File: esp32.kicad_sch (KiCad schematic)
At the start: 8 parts, among them U1 ESP32-S3-WROOM-2, U4 74HC595, U6 TCA9548APWR

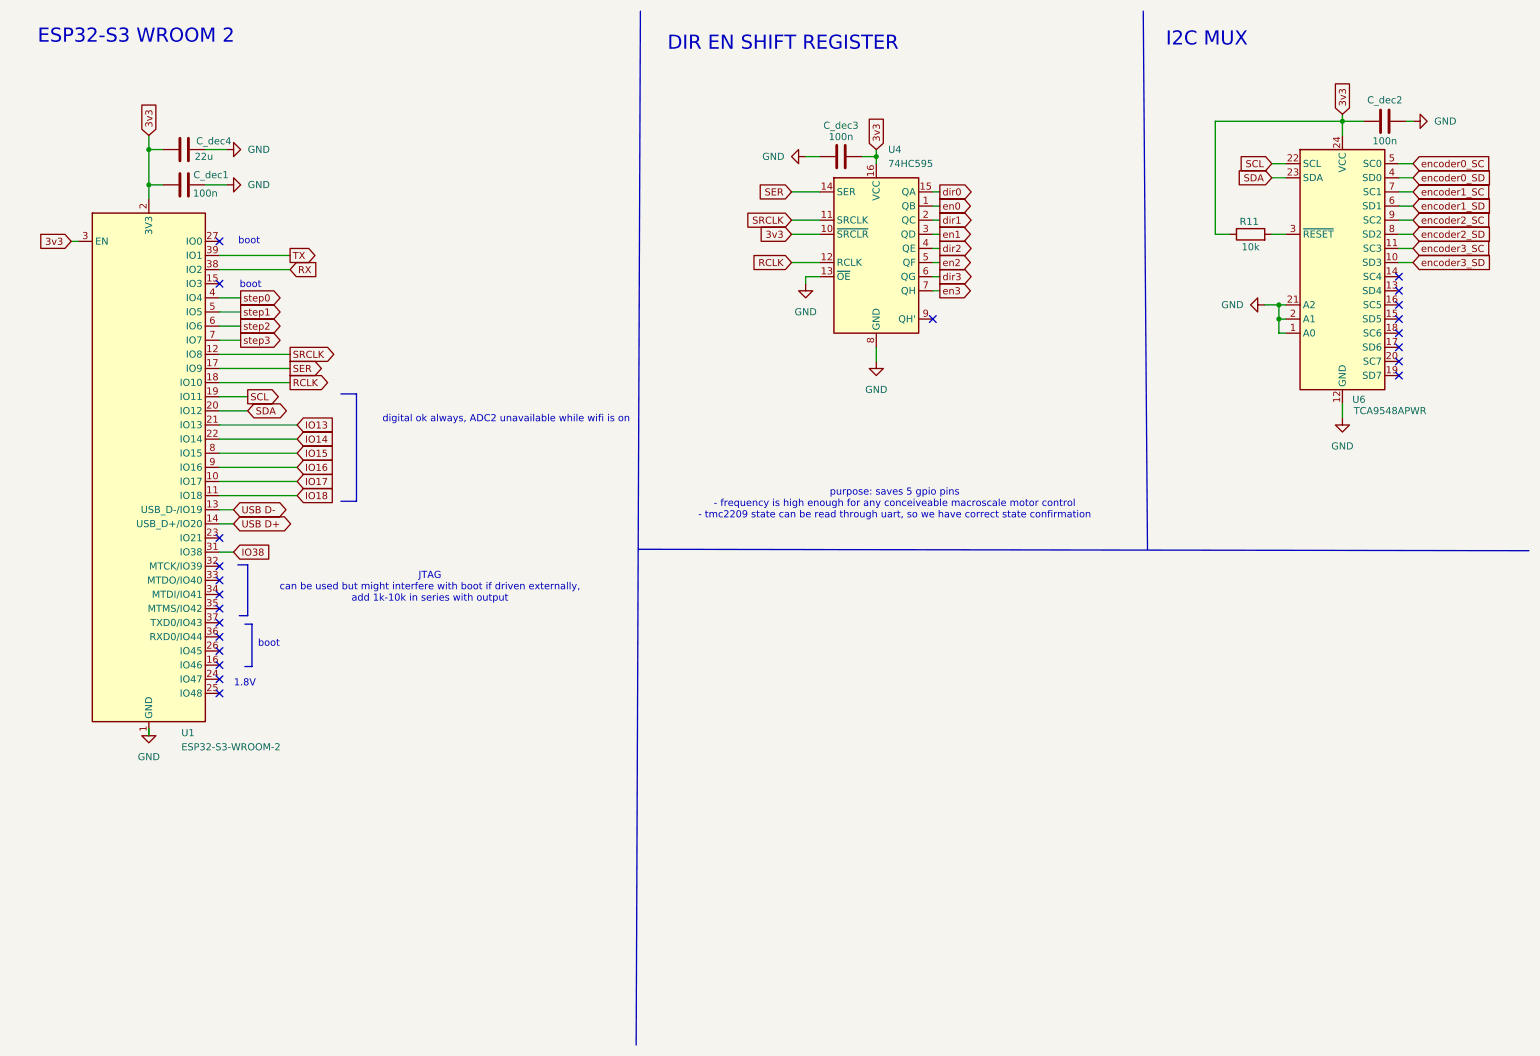
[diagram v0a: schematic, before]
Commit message: revision 1: I2C pullups, USB LDO, etc.
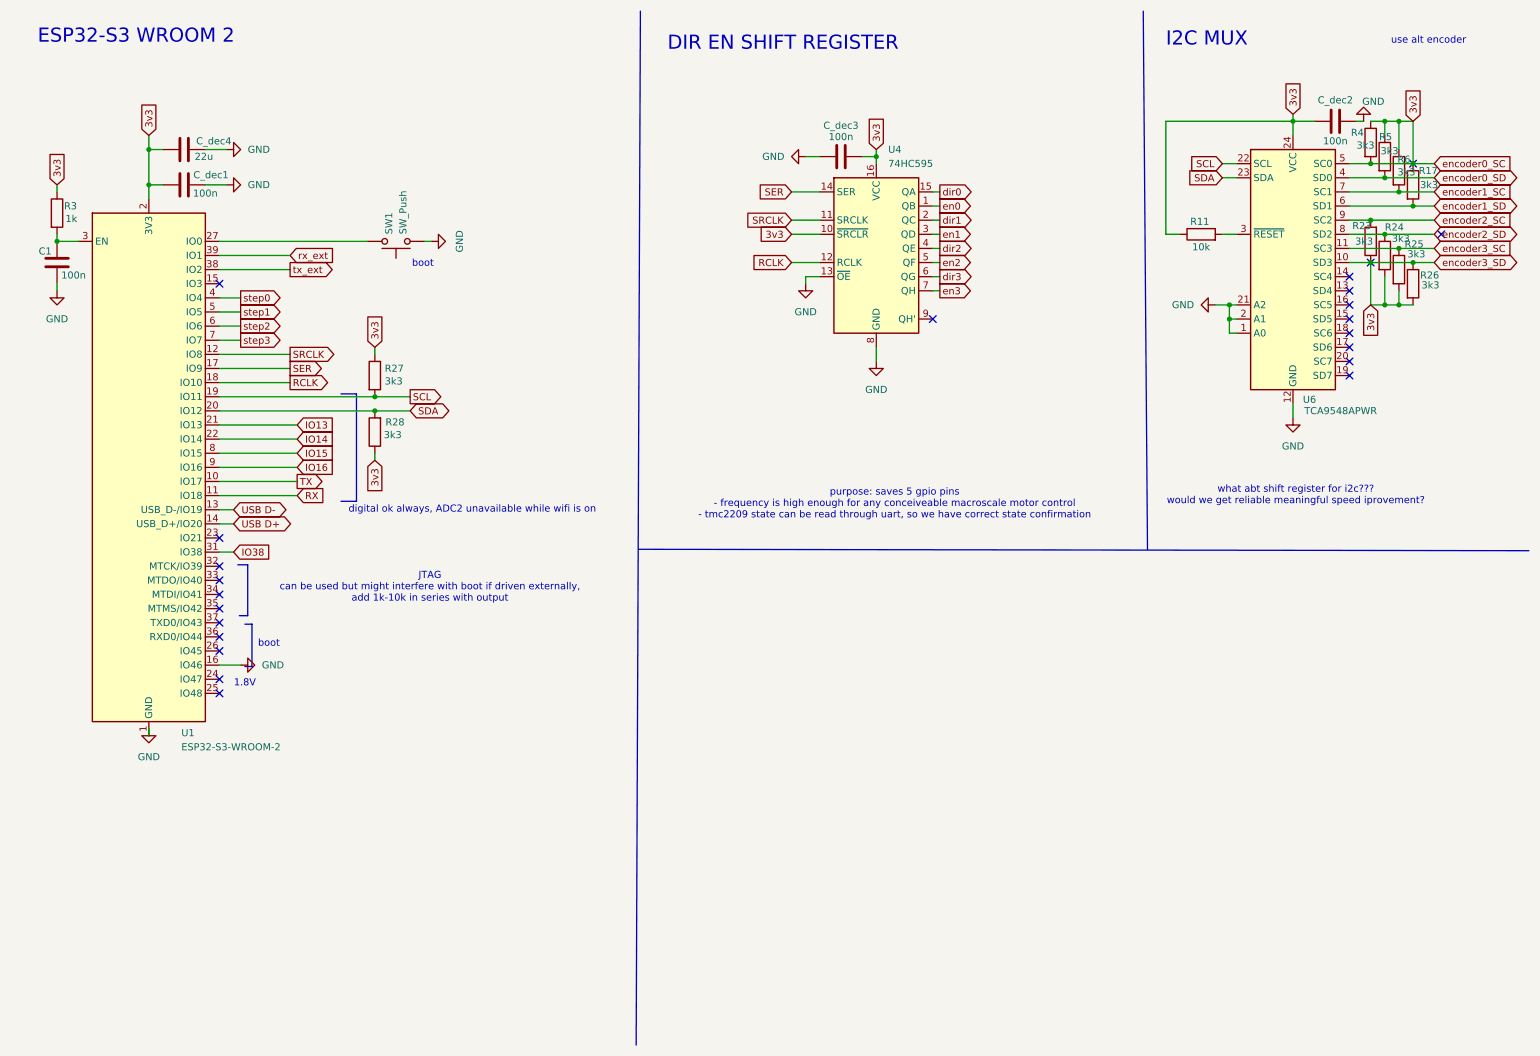
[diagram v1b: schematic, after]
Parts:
- added C1: 100n, symbol Device:C
- added R17, R23, R24, R25, R26, R27, R28, R4, R5, R6: 3k3, symbol Device:R
- added R3: 1k, symbol Device:R
- added SW1: SW_Push, symbol Switch:SW_Push
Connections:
- net IO17 is gone; now on net TX: U1.10 (IO17)
- net IO18 is gone; now on net RX: U1.11 (IO18)
- net encoder0_SC is gone; now on net 3v3: U6.5 (SC0)
- net encoder3_SD is gone; now on net 3v3: U6.10 (SD3)
- net 3v3: now also R17.1, R23.1, R24.2, R25.2, R26.1, R26.2, R27.1, R28.1, R3.1, R4.1, R4.2, R5.1, R6.1; no longer U1.3 (EN)
- net GND: now also U1.16 (IO46), C1.2, SW1.1
- net RX: no longer U1.38 (IO2)
- net SCL: now also R27.2
- net SDA: now also R28.2
- net TX: no longer U1.39 (IO1)
- net encoder0_SD: now also R5.2
- net encoder1_SC: now also R6.2
- net encoder1_SD: now also R17.2
- net encoder2_SC: now also R23.2
- net encoder2_SD: now also R24.1
- net encoder3_SC: now also R25.1
- net at U1.27 (IO0): now also SW1.2
- new net: C1.1, R3.2, U1.3 (EN)
- new net rx_ext: U1.39 (IO1)
- new net tx_ext: U1.38 (IO2)
- no-connect marks 22 -> 23
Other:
- note added: "use alt encoder"
- note added: "what abt shift register for i2c??? would we get reliable meaningful speed iprovement?"
- moved on the sheet: C_dec2, R11, U6
